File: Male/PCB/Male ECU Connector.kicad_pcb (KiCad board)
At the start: 2 copper layers, 22 x 135 mm, 3 parts, among them J1 DJetECUEdgeConnector, J2 SOLDER HOLES, J3 SOLDER HOLES

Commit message: Converted project to KiCAD 6.
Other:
- net class 2A removed
- net class 4A removed
- net class Default removed

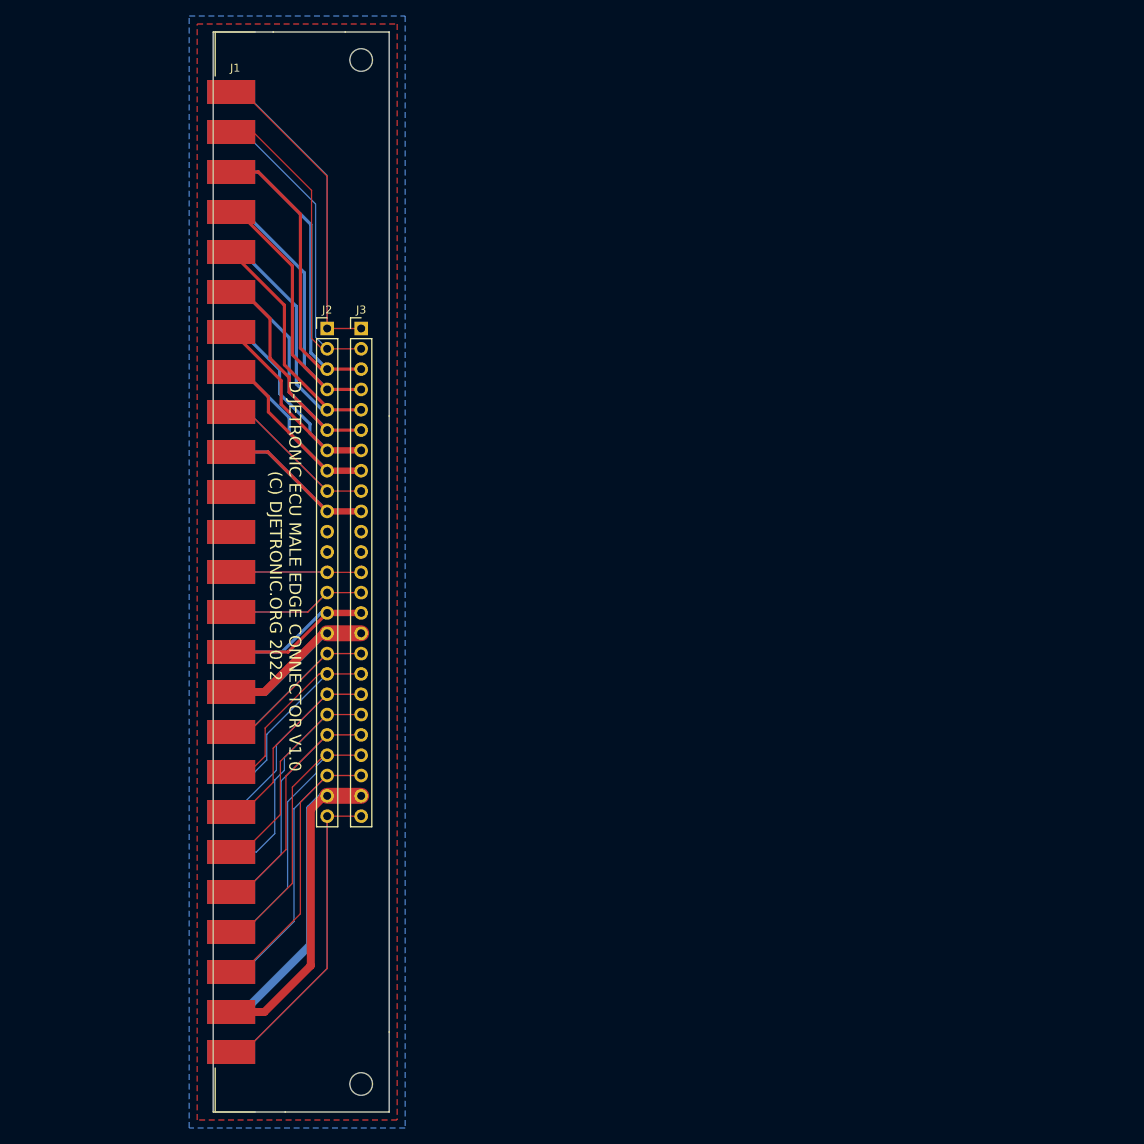
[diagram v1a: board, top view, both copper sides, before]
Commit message: Added relay to disable fuel pump.
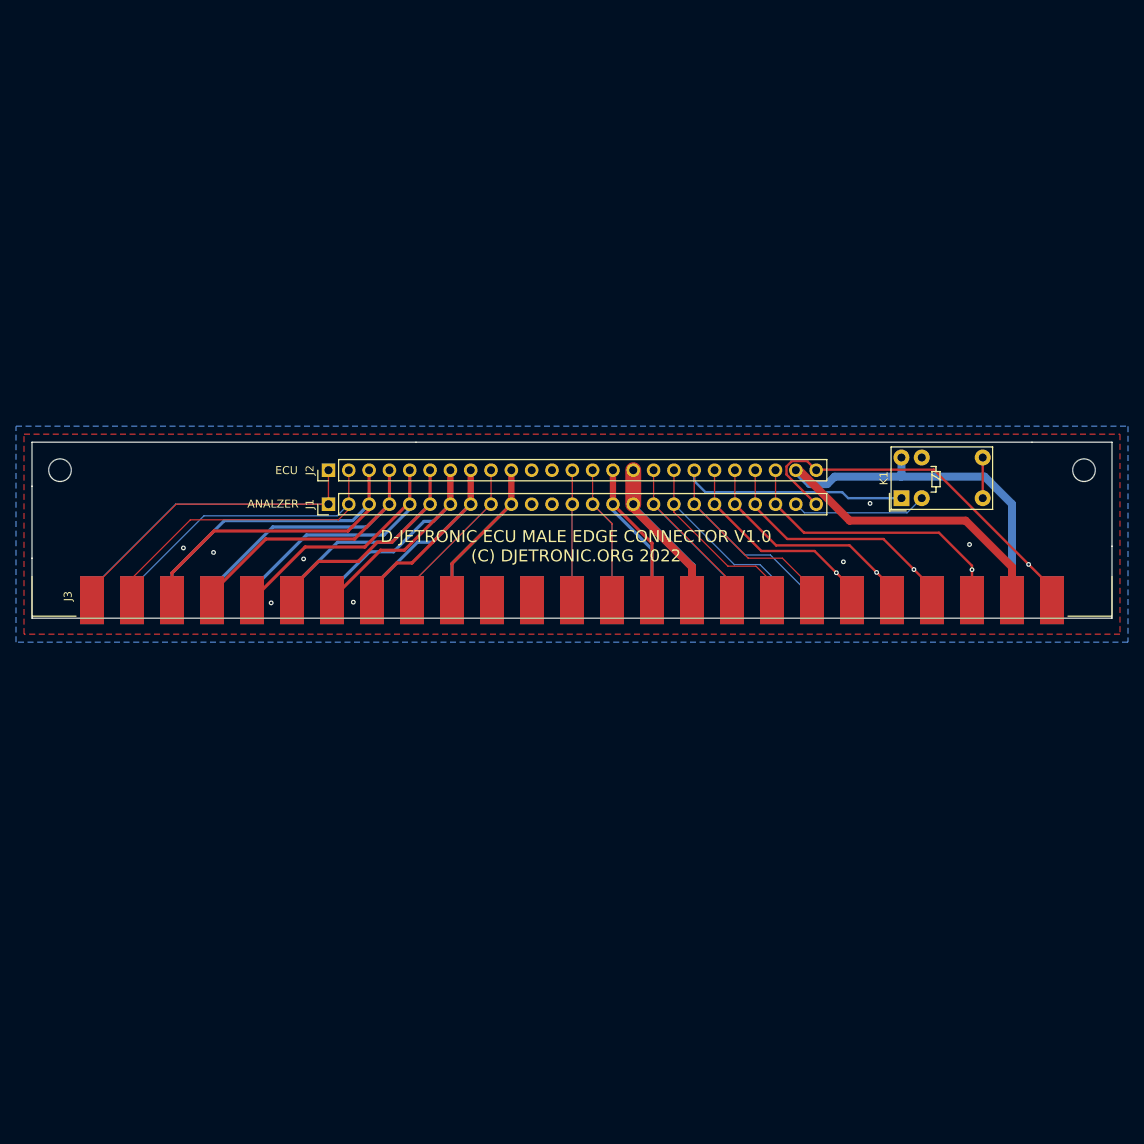
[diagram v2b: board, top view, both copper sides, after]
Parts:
- added K1: G5V-1-DC5, Relay_THT:Relay_SPDT_Omron_G5V-1, F.Cu at (190.5, 94.3)
- J1: renamed from J2; value SOLDER HOLES -> ANALYZER
- J2: renamed from J3; value SOLDER HOLES -> ECU
- moved J3 65.9 mm to (89.4, 107.0), turned to 90 degrees
- moved J1 22.0 mm to (118.9, 95.0), turned to 90 degrees
- moved J2 18.2 mm to (118.9, 90.8), turned to 90 degrees
- renumbered J1 to J3
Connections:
- net Net-(J1-PadA19) renamed /ECU_FUEL_PUMP_CTRL
- J1 pad 12: /GND -> unconnected-(J1-Pad12)
- J1 pad 24: /12V_2 -> /FUEL_PUMP_DISABLE
- J2 pad 24: /12V_2 -> /12V_1
- J3 pad A24: /12V_2 -> /12V_1
- J3 pad B24: /12V_2 -> /12V_1
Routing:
- net /12V_1: track 34.3 -> 114.9 mm
- net /12V_2: track 72.0 -> 0.00 mm
- net /ECU_FUEL_PUMP_CTRL: track 44.8 -> 72.9 mm
- net Net-(J1-Pad23): track 65.0 -> 41.5 mm, vias 0 -> 1
- net Net-(J1-Pad22): track 60.4 -> 37.2 mm, vias 0 -> 1
- net Net-(J1-Pad25): track 75.0 -> 53.6 mm, vias 0 -> 1
- net Net-(J1-Pad21): track 55.3 -> 34.0 mm, vias 0 -> 1
- net Net-(J1-Pad20): track 51.3 -> 31.5 mm, vias 0 -> 1
- net /FUEL_PUMP_DISABLE: track 0.00 -> 17.3 mm
- net /FUEL_PUMP_RELAY: track 0.00 -> 5.08 mm
- net /GND: vias 0 -> 8
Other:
- board size 22 x 135 mm -> 135 x 22 mm
- board text added: "ANALZER"
- board text added: "ECU"

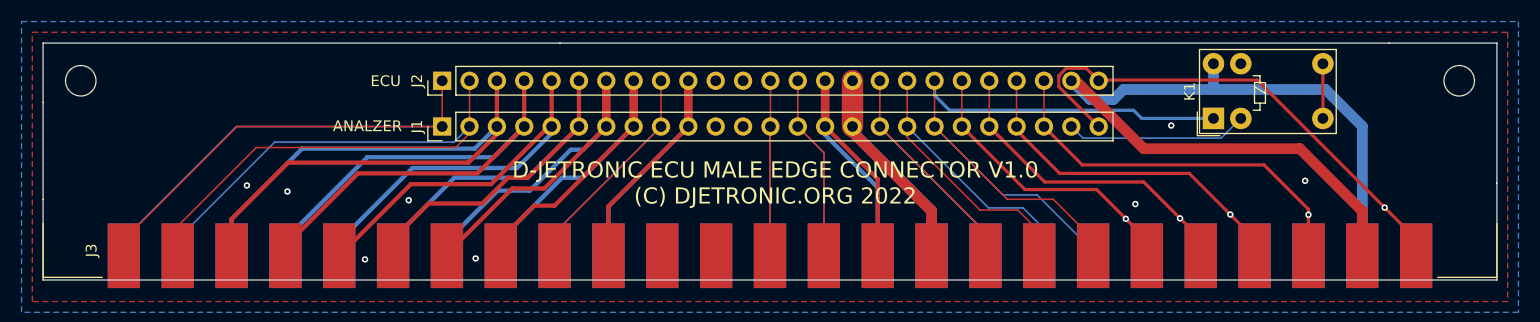
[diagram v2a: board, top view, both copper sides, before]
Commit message: Added larger holes for 18AWG (0.75mm2) engine harness wires. Rounded back corners of PCB to make it easier to design case. Added solder jumper to make relay optional.
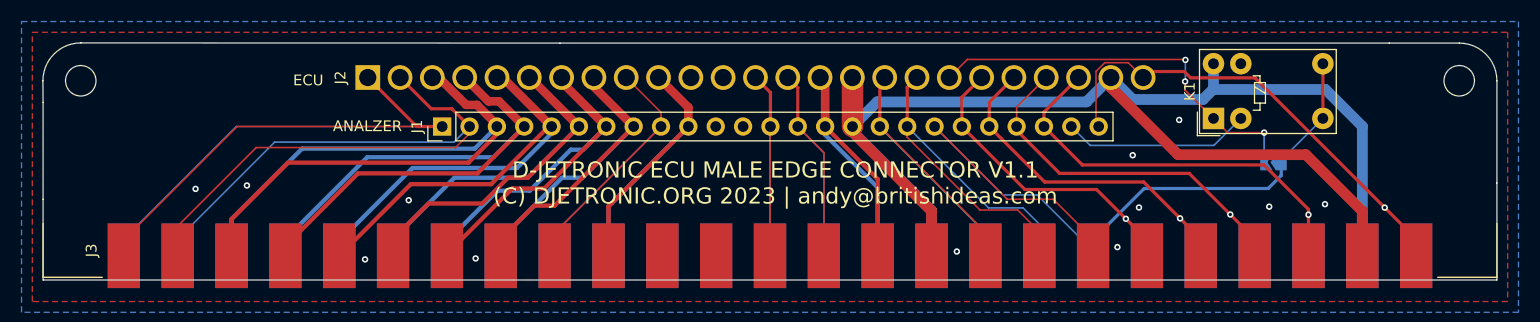
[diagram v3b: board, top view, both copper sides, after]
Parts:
- added JP1: NO_RELAY, Jumper:SolderJumper-2_P1.3mm_Open_TrianglePad1.0x1.5mm, B.Cu at (196.1, 98.3)
- J2: footprint Connector_PinHeader_2.54mm:PinHeader_1x25_P2.54mm_Vertical -> Britishideas:Pins_1x25_P3.00mm_18AWG
- moved J2 6.92 mm to (112.0, 90.5)
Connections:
- J1 pad 19: /ECU_FUEL_PUMP_CTRL -> /FUEL_PUMP_RELAY
- J3 pad A19: /ECU_FUEL_PUMP_CTRL -> /FUEL_PUMP_RELAY
- J3 pad B19: /ECU_FUEL_PUMP_CTRL -> /FUEL_PUMP_RELAY
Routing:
- net /FUEL_PUMP_RELAY: track 5.08 -> 72.4 mm
- net /ECU_FUEL_PUMP_CTRL: track 72.9 -> 37.2 mm, vias 0 -> 3
- net /12V_1: track 114.9 -> 133.8 mm
- net Net-(J1-Pad1): track 75.1 -> 79.6 mm
- net Net-(J1-Pad2): track 71.3 -> 75.4 mm
- net Net-(J1-Pad25): track 53.6 -> 49.8 mm
- net /INJI: track 67.9 -> 71.6 mm
- net /INJIII: track 60.0 -> 63.2 mm
- net /INJII: track 54.8 -> 57.5 mm
- net /INJIV: track 50.5 -> 52.8 mm
- net Net-(J1-Pad7): track 44.7 -> 46.8 mm
- net Net-(J1-Pad17): track 36.4 -> 34.7 mm
- net Net-(J1-Pad9): track 36.4 -> 38.1 mm
- net Net-(J1-Pad18): track 42.3 -> 40.8 mm
- net Net-(J1-Pad8): track 41.0 -> 42.5 mm
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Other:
- outline, holes or cut-outs redrawn
- board text added: "D-JETRONIC ECU MALE EDGE CONNECTOR V1.1 (C) DJETRONIC.ORG 2023 | andy@britishideas.com"
- board text removed: "D-JETRONIC ECU MALE EDGE CONNECTOR V1.0 (C) DJETRONIC.ORG 2022"

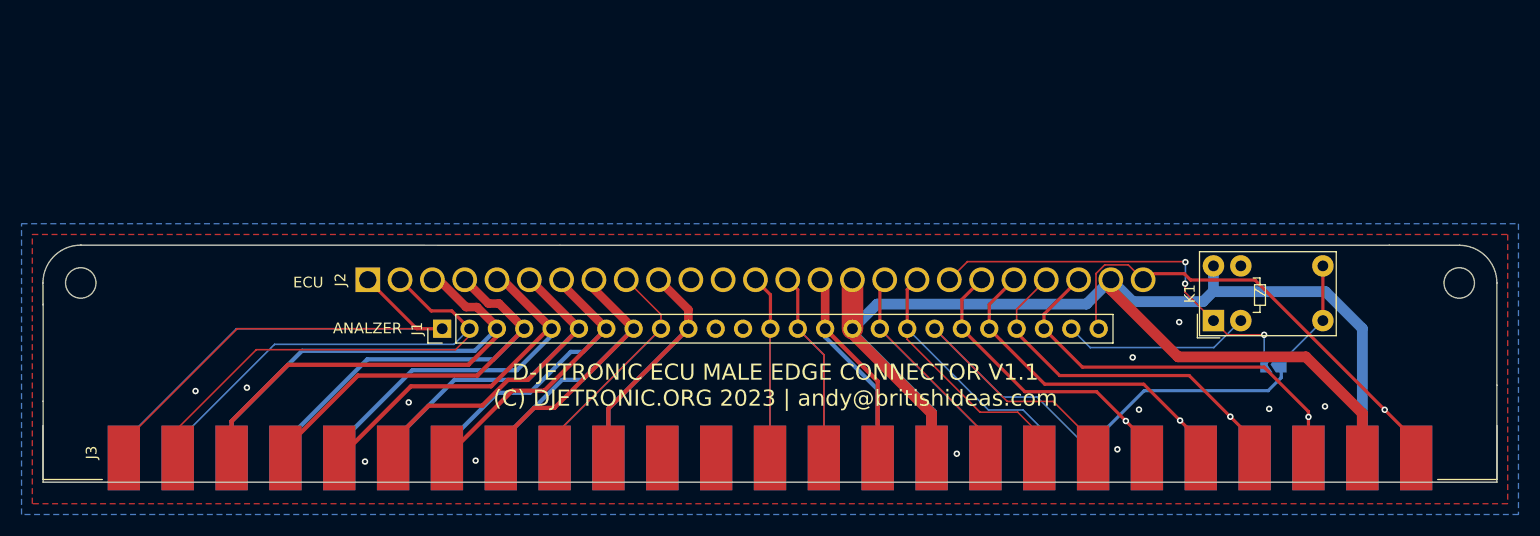
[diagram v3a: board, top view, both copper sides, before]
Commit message: Laid out PCB fpr male connector.
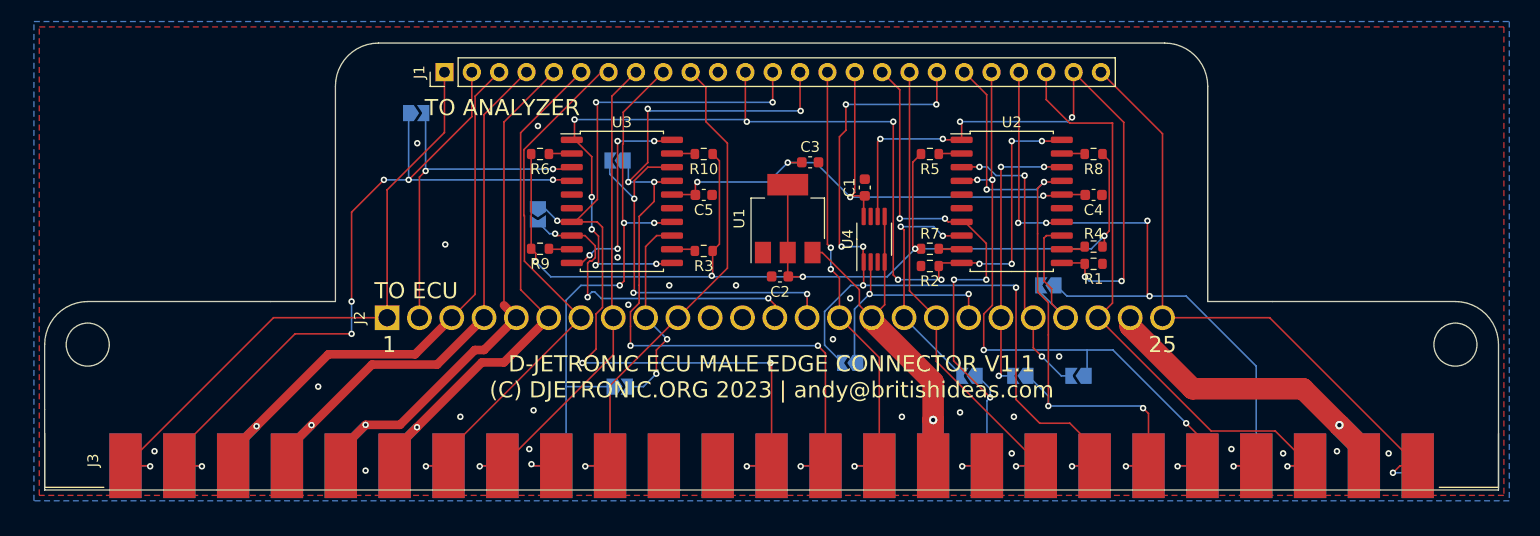
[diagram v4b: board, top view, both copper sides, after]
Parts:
- removed K1: G5V-1-DC5, Relay_THT:Relay_SPDT_Omron_G5V-1
- added C1: 1u, Capacitor_SMD:C_0603_1608Metric, F.Cu at (158.2, 81.9)
- added C2: 2u2, Capacitor_SMD:C_0603_1608Metric, F.Cu at (150.3, 90.2)
- added C3: 100nF, Capacitor_SMD:C_0603_1608Metric, F.Cu at (153.1, 79.6)
- added C4: 100nF, Capacitor_SMD:C_0603_1608Metric, F.Cu at (179.4, 82.6)
- added C5: 100nF, Capacitor_SMD:C_0603_1608Metric, F.Cu at (143.2, 82.6)
- added JP2: NO_ANALYZER, Jumper:SolderJumper-2_P1.3mm_Open_TrianglePad1.0x1.5mm, B.Cu at (178.0, 99.4)
- added JP3: NO_ANALYZER, Jumper:SolderJumper-2_P1.3mm_Open_TrianglePad1.0x1.5mm, B.Cu at (175.2, 91.0)
- added JP4: NO_ANALYZER, Jumper:SolderJumper-2_P1.3mm_Open_TrianglePad1.0x1.5mm, B.Cu at (116.5, 75.0)
- added JP5: NO_ANALYZER, Jumper:SolderJumper-2_P1.3mm_Open_TrianglePad1.0x1.5mm, B.Cu at (135.4, 100.4)
- added JP6: NO_ANALYZER, Jumper:SolderJumper-2_P1.3mm_Open_TrianglePad1.0x1.5mm, B.Cu at (167.9, 99.4)
- added JP7: NO_ANALYZER, Jumper:SolderJumper-2_P1.3mm_Open_TrianglePad1.0x1.5mm, B.Cu at (172.6, 99.4)
- added JP8: NO_ANALYZER, Jumper:SolderJumper-2_P1.3mm_Open_TrianglePad1.0x1.5mm, B.Cu at (127.8, 84.4)
- added JP9: NO_ANALYZER, Jumper:SolderJumper-2_P1.3mm_Open_TrianglePad1.0x1.5mm, B.Cu at (135.2, 79.4)
- added R1: 10K, Resistor_SMD:R_0603_1608Metric, F.Cu at (179.4, 89.0)
- added R10: 10K, Resistor_SMD:R_0603_1608Metric, F.Cu at (143.2, 78.8)
- added R2: 10K, Resistor_SMD:R_0603_1608Metric, F.Cu at (164.2, 89.2)
- added R3: 10K, Resistor_SMD:R_0603_1608Metric, F.Cu at (143.2, 87.8)
- added R4: 10K, Resistor_SMD:R_0603_1608Metric, F.Cu at (179.4, 87.4)
- added R5: 10K, Resistor_SMD:R_0603_1608Metric, F.Cu at (164.2, 78.8)
- added R6: 10K, Resistor_SMD:R_0603_1608Metric, F.Cu at (128.0, 78.8)
- added R7: 10K, Resistor_SMD:R_0603_1608Metric, F.Cu at (164.2, 87.6)
- added R8: 10K, Resistor_SMD:R_0603_1608Metric, F.Cu at (179.4, 78.8)
- added R9: 10K, Resistor_SMD:R_0603_1608Metric, F.Cu at (128.0, 87.6)
- added U1: TLV76150DCYR, Package_TO_SOT_SMD:SOT-223-3_TabPin2, F.Cu at (151.0, 84.8)
- added U2: DG333ADW-T1-E3, Package_SO:SOIC-20W_7.5x12.8mm_P1.27mm, F.Cu at (171.8, 83.2)
- added U3: DG333ADW-T1-E3, Package_SO:SOIC-20W_7.5x12.8mm_P1.27mm, F.Cu at (135.6, 83.2)
- added U4: DG419BDQ-T1-E3, Package_SO:MSOP-8_3x3mm_P0.65mm, F.Cu at (159.0, 86.7)
- JP1: value NO_RELAY -> NO_ANALYZER
- moved JP1 39.3 mm to (156.8, 98.2)
- moved J1 23.8 mm to (119.1, 71.2)
- moved J2 3.96 mm to (113.8, 94.0)
- moved J3 0.74 mm to (89.5, 107.8)
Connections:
- J1 pad 12: unconnected-(J1-Pad12) -> /TPS_DISABLE
- J1 pad 13: Net-(J1-Pad13) -> /PGII
- J1 pad 14: Net-(J1-Pad14) -> /PGIV
- J1 pad 17: Net-(J1-Pad17) -> /TPS_IDLE
- J1 pad 2: Net-(J1-Pad2) -> /TPS_WOT_DIAG_II_IV
- J1 pad 20: Net-(J1-Pad20) -> /TPS_ACCEL2
- J1 pad 21: Net-(J1-Pad21) -> /PGI
- J1 pad 22: Net-(J1-Pad22) -> /PGIII
- J1 pad 24: /FUEL_PUMP_DISABLE -> /FUEL_PUMP_PG_DISABLE
- J1 pad 9: Net-(J1-Pad9) -> /TPS_ACCEL1
- J2 pad 13: Net-(J1-Pad13) -> /ECU_PGII
- J2 pad 14: Net-(J1-Pad14) -> /ECU_PGIV
- J2 pad 17: Net-(J1-Pad17) -> /ECU_TPS_IDLE
- J2 pad 2: Net-(J1-Pad2) -> /ECU_TPS_WOT_DIAG_II_IV
- J2 pad 20: Net-(J1-Pad20) -> /ECU_TPS_ACCEL2
- J2 pad 21: Net-(J1-Pad21) -> /ECU_PGI
- J2 pad 22: Net-(J1-Pad22) -> /ECU_PGIII
- J2 pad 24: /12V_1 -> /12V_2
- J2 pad 9: Net-(J1-Pad9) -> /ECU_TPS_ACCEL1
- J3 pad A13: Net-(J1-Pad13) -> /PGII
- J3 pad A14: Net-(J1-Pad14) -> /PGIV
- J3 pad A17: Net-(J1-Pad17) -> /TPS_IDLE
- J3 pad A2: Net-(J1-Pad2) -> /TPS_WOT_DIAG_II_IV
- J3 pad A20: Net-(J1-Pad20) -> /TPS_ACCEL2
- J3 pad A21: Net-(J1-Pad21) -> /PGI
- J3 pad A22: Net-(J1-Pad22) -> /PGIII
- J3 pad A24: /12V_1 -> /12V_2
- J3 pad A9: Net-(J1-Pad9) -> /TPS_ACCEL1
- J3 pad B13: Net-(J1-Pad13) -> /PGII
- J3 pad B14: Net-(J1-Pad14) -> /PGIV
- J3 pad B17: Net-(J1-Pad17) -> /TPS_IDLE
- J3 pad B2: Net-(J1-Pad2) -> /TPS_WOT_DIAG_II_IV
- J3 pad B20: Net-(J1-Pad20) -> /TPS_ACCEL2
- J3 pad B21: Net-(J1-Pad21) -> /PGI
- J3 pad B22: Net-(J1-Pad22) -> /PGIII
- J3 pad B24: /12V_1 -> /12V_2
- J3 pad B9: Net-(J1-Pad9) -> /TPS_ACCEL1
- JP1 pad 1: /FUEL_PUMP_RELAY -> /ECU_FUEL_PUMP_CTRL
- JP1 pad 2: /ECU_FUEL_PUMP_CTRL -> /FUEL_PUMP_RELAY
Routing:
- net +5V: track 0.00 -> 105.8 mm, vias 0 -> 5
- net /TPS_DISABLE: track 0.00 -> 99.8 mm, vias 0 -> 13
- net /PGII: track 0.00 -> 83.4 mm, vias 0 -> 6
- net /PGIV: track 0.00 -> 81.3 mm, vias 0 -> 7
- net /FUEL_PUMP_PG_DISABLE: track 0.00 -> 79.7 mm, vias 0 -> 10
- net /TPS_WOT_DIAG_II_IV: track 0.00 -> 79.4 mm, vias 0 -> 6
- net Net-(J1-Pad2): track 75.4 -> 0.00 mm
- net /PGIII: track 0.00 -> 69.9 mm, vias 0 -> 5
- net /TPS_ACCEL2: track 0.00 -> 62.8 mm, vias 0 -> 5
- net /PGI: track 0.00 -> 62.3 mm, vias 0 -> 5
- net /TPS_ACCEL1: track 0.00 -> 56.4 mm, vias 0 -> 4
- net /TPS_IDLE: track 0.00 -> 55.6 mm, vias 0 -> 6
- net Net-(J1-Pad9): track 38.1 -> 0.00 mm
- net /ECU_PGIV: track 0.00 -> 37.3 mm, vias 0 -> 3
- net Net-(J1-Pad22): track 37.1 -> 0.00 mm, vias 1 -> 0
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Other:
- board size 135 x 22 mm -> 135 x 41.5 mm
- board text added: "1"
- board text added: "25"
- board text added: "SOLDER ALL JUMPERS IF NO ANALYZER AND TOP COMPONENTS ARE NOT POPULATED"
- board text added: "TO ANALYZER"
- board text added: "TO ECU"
- board text removed: "ANALZER"
- board text removed: "ECU"

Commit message: Completed PCB design for male connector.
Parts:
- added FID1: Fiducial, Fiducial:Fiducial_0.5mm_Mask1.5mm, F.Cu at (94.1, 96.1)
- added FID2: Fiducial, Fiducial:Fiducial_0.5mm_Mask1.5mm, F.Cu at (204.3, 96.0)
- added FID3: Fiducial, Fiducial:Fiducial_0.5mm_Mask1.5mm, F.Cu at (184.3, 72.9)
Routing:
- net /FUEL_PUMP_PG_DISABLE: track 79.7 -> 99.3 mm, vias 10 -> 11
- net /12V_1: track 97.2 -> 100.6 mm
- net Net-(J1-Pad1): track 61.2 -> 59.6 mm
- net /ECU_TPS_ACCEL1: track 19.1 -> 20.1 mm
- net /PGII: track 83.4 -> 84.4 mm
- net /TPS_ACCEL1: track 56.4 -> 57.0 mm
- net /FUEL_PUMP_RELAY: track 80.4 -> 81.0 mm
- net /TPS_IDLE: track 55.6 -> 56.1 mm
- net /GND: vias 24 -> 89
